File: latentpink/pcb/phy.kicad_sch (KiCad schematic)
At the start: 72 parts, among them J1 CONN_SFP_HOST, J18 BEL_FUSE_0845-2R1T-E4, J19 BEL_FUSE_0845-2R1T-E4, J2 SFP_CAGE, J20 BEL_FUSE_0845-2R1T-E4, J21 BEL_FUSE_0845-2R1T-E4, J3 XILINX_JTAG, J4 BEL_FUSE_0845-2R1T-E4, J8 BEL_FUSE_0845-2R1T-E4, M1 960-27-12-D-AB-0, U1 VSC8512, U2 XC7K160T-2FBG484C, U24 OSC_LVDS, U25 OSC_LVDS, U4 STM32H735-UFBGA176-25

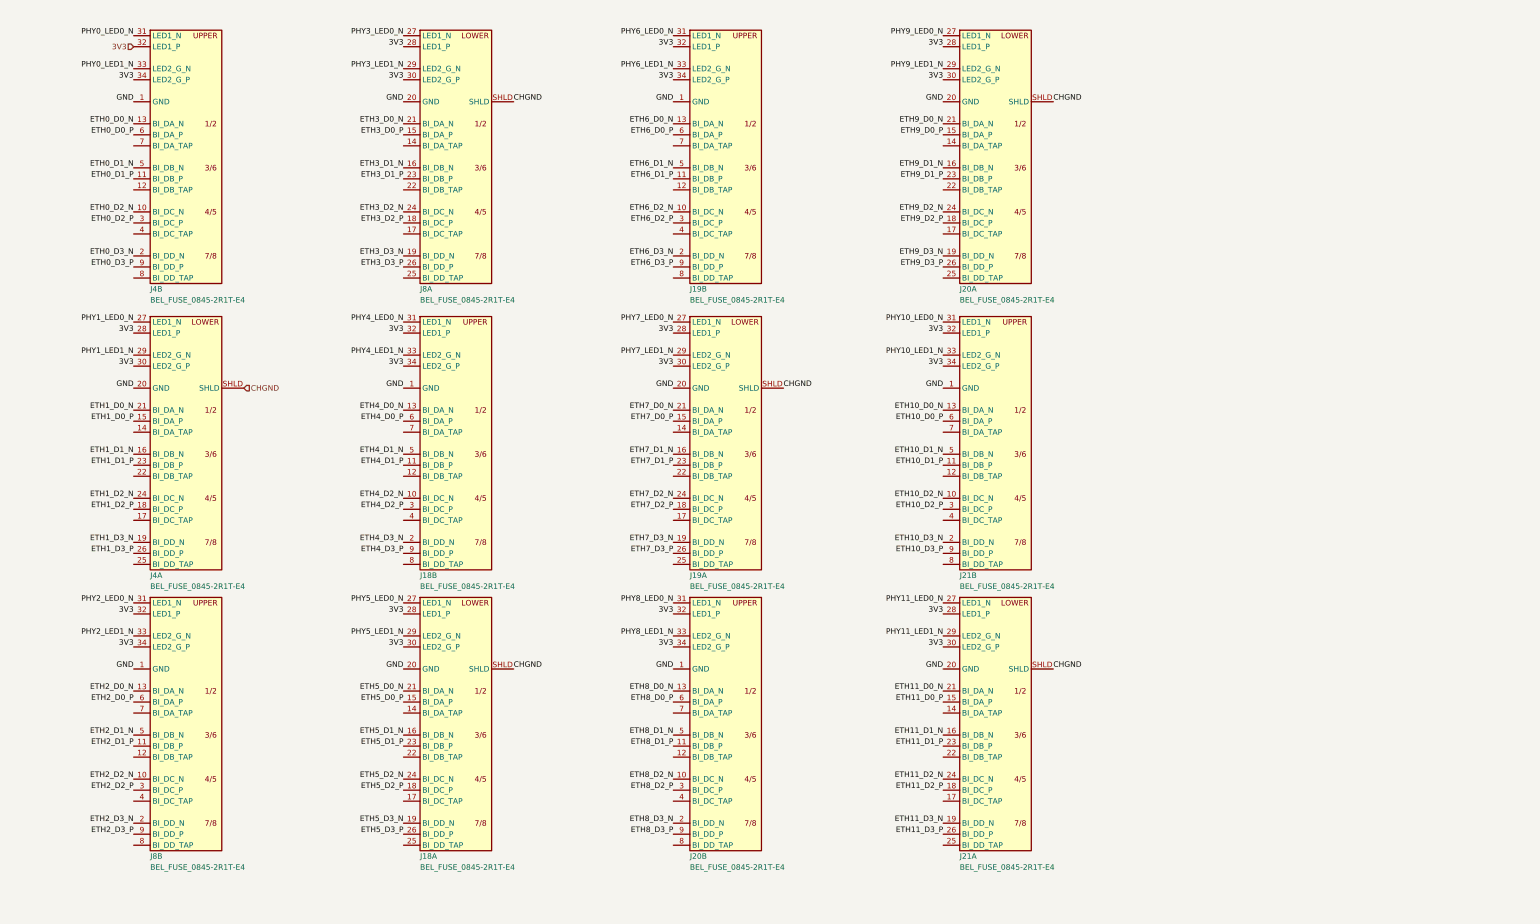
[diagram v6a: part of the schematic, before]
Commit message: Rearranged ports, added center tap capacitors
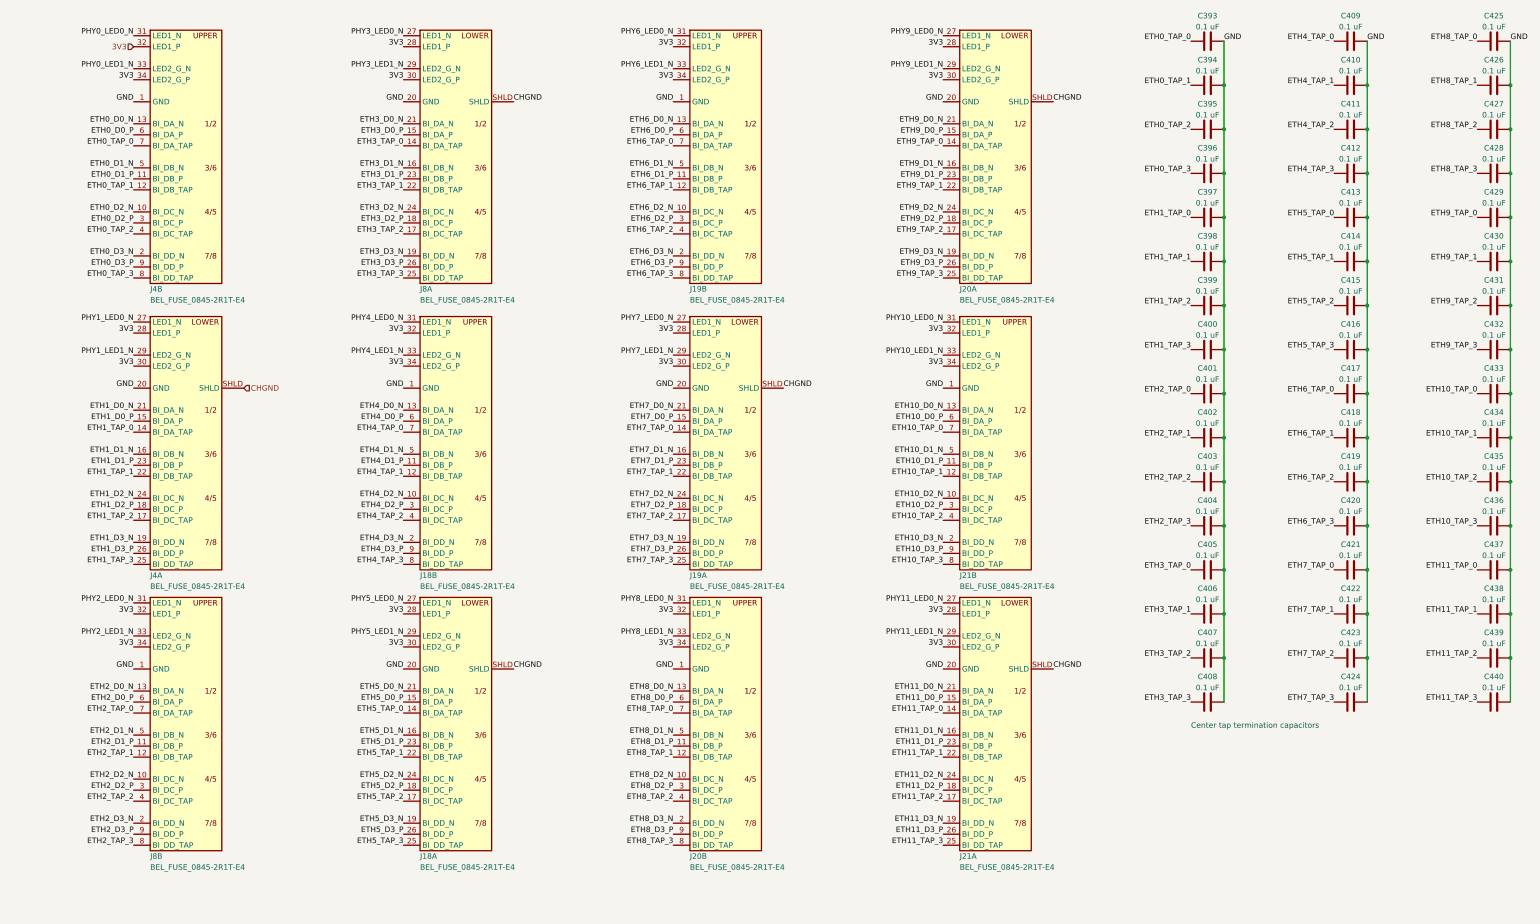
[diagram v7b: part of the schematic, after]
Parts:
- added C393, C394, C395, C396, C397, C398, C399, C400, C401, C402, C403, C404, C405, C406, C407, C408, C409, C410, C411, C412, C413, C414, C415, C416, C417, C418, C419, C420, C421, C422, C423, C424, C425, C426, C427, C428, C429, C430, C431, C432, C433, C434, C435, C436, C437, C438, C439, C440: 0.1 uF, azonenberg_pcb:EIA_0402_CAP_NOSILK, symbol device:C
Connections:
- net GND: now also C393.1, C394.1, C395.1, C396.1, C397.1, C398.1, C399.1, C400.1, C401.1, C402.1, C403.1, C404.1, C405.1, C406.1, C407.1, C408.1, C409.1, C410.1, C411.1, C412.1, C413.1, C414.1, C415.1, C416.1, C417.1, C418.1, C419.1, C420.1, C421.1, C422.1, C423.1, C424.1, C425.1, C426.1, C427.1, C428.1, C429.1, C430.1, C431.1, C432.1, C433.1, C434.1, C435.1, C436.1, C437.1, C438.1, C439.1, C440.1
- net ETH0_TAP_1: now reaches J4.12 (BI_DB_TAP)
- net ETH0_TAP_1: now also C394.2
- net ETH0_TAP_2: now reaches J4.4 (BI_DC_TAP)
- net ETH0_TAP_2: now also C395.2
- net ETH0_TAP_0: now reaches J4.7 (BI_DA_TAP)
- net ETH0_TAP_0: now also C393.2
- net ETH0_TAP_3: now reaches J4.8 (BI_DD_TAP)
- net ETH0_TAP_3: now also C396.2
- net ETH10_TAP_1: now reaches J21.12 (BI_DB_TAP)
- net ETH10_TAP_1: now also C434.2
- net ETH10_TAP_2: now reaches J21.4 (BI_DC_TAP)
- net ETH10_TAP_2: now also C435.2
- net ETH10_TAP_0: now reaches J21.7 (BI_DA_TAP)
- net ETH10_TAP_0: now also C433.2
- net ETH10_TAP_3: now reaches J21.8 (BI_DD_TAP)
- net ETH10_TAP_3: now also C436.2
- net ETH8_TAP_1: now reaches J20.12 (BI_DB_TAP)
- net ETH8_TAP_1: now also C426.2
- net ETH8_TAP_2: now reaches J20.4 (BI_DC_TAP)
- net ETH8_TAP_2: now also C427.2
- net ETH8_TAP_0: now reaches J20.7 (BI_DA_TAP)
- net ETH8_TAP_0: now also C425.2
- net ETH8_TAP_3: now reaches J20.8 (BI_DD_TAP)
- net ETH8_TAP_3: now also C428.2
- net ETH2_TAP_1: now reaches J8.12 (BI_DB_TAP)
- net ETH2_TAP_1: now also C402.2
- net ETH2_TAP_2: now reaches J8.4 (BI_DC_TAP)
- net ETH2_TAP_2: now also C403.2
- net ETH2_TAP_0: now reaches J8.7 (BI_DA_TAP)
- net ETH2_TAP_0: now also C401.2
- net ETH2_TAP_3: now reaches J8.8 (BI_DD_TAP)
- net ETH2_TAP_3: now also C404.2
- net ETH3_TAP_0: now reaches J8.14 (BI_DA_TAP)
- net ETH3_TAP_0: now also C405.2
- net ETH3_TAP_2: now reaches J8.17 (BI_DC_TAP)
- net ETH3_TAP_2: now also C407.2
- net ETH3_TAP_1: now reaches J8.22 (BI_DB_TAP)
- net ETH3_TAP_1: now also C406.2
- net ETH3_TAP_3: now reaches J8.25 (BI_DD_TAP)
- net ETH3_TAP_3: now also C408.2
- net ETH5_TAP_0: now reaches J18.14 (BI_DA_TAP)
- net ETH5_TAP_0: now also C413.2
- net ETH5_TAP_2: now reaches J18.17 (BI_DC_TAP)
- net ETH5_TAP_2: now also C415.2
- net ETH5_TAP_1: now reaches J18.22 (BI_DB_TAP)
- net ETH5_TAP_1: now also C414.2
- net ETH5_TAP_3: now reaches J18.25 (BI_DD_TAP)
- net ETH5_TAP_3: now also C416.2
- net ETH6_TAP_1: now reaches J19.12 (BI_DB_TAP)
- net ETH6_TAP_1: now also C418.2
- net ETH6_TAP_2: now reaches J19.4 (BI_DC_TAP)
- net ETH6_TAP_2: now also C419.2
- net ETH6_TAP_0: now reaches J19.7 (BI_DA_TAP)
- net ETH6_TAP_0: now also C417.2
- net ETH6_TAP_3: now reaches J19.8 (BI_DD_TAP)
- net ETH6_TAP_3: now also C420.2
- net ETH4_TAP_1: now reaches J18.12 (BI_DB_TAP)
- net ETH4_TAP_1: now also C410.2
- net ETH4_TAP_2: now reaches J18.4 (BI_DC_TAP)
- net ETH4_TAP_2: now also C411.2
- net ETH4_TAP_0: now reaches J18.7 (BI_DA_TAP)
- net ETH4_TAP_0: now also C409.2
- net ETH4_TAP_3: now reaches J18.8 (BI_DD_TAP)
- net ETH4_TAP_3: now also C412.2
- net ETH1_TAP_0: now reaches J4.14 (BI_DA_TAP)
- net ETH1_TAP_0: now also C397.2
- net ETH1_TAP_2: now reaches J4.17 (BI_DC_TAP)
- net ETH1_TAP_2: now also C399.2
- net ETH1_TAP_1: now reaches J4.22 (BI_DB_TAP)
- net ETH1_TAP_1: now also C398.2
- net ETH1_TAP_3: now reaches J4.25 (BI_DD_TAP)
- net ETH1_TAP_3: now also C400.2
- net ETH9_TAP_0: now reaches J20.14 (BI_DA_TAP)
- net ETH9_TAP_0: now also C429.2
- net ETH9_TAP_2: now reaches J20.17 (BI_DC_TAP)
- net ETH9_TAP_2: now also C431.2
- net ETH9_TAP_1: now reaches J20.22 (BI_DB_TAP)
- net ETH9_TAP_1: now also C430.2
- net ETH9_TAP_3: now reaches J20.25 (BI_DD_TAP)
- net ETH9_TAP_3: now also C432.2
- net ETH7_TAP_0: now reaches J19.14 (BI_DA_TAP)
- net ETH7_TAP_0: now also C421.2
- net ETH7_TAP_2: now reaches J19.17 (BI_DC_TAP)
- net ETH7_TAP_2: now also C423.2
- net ETH7_TAP_1: now reaches J19.22 (BI_DB_TAP)
- net ETH7_TAP_1: now also C422.2
- net ETH7_TAP_3: now reaches J19.25 (BI_DD_TAP)
- net ETH7_TAP_3: now also C424.2
- net ETH11_TAP_0: now reaches J21.14 (BI_DA_TAP)
- net ETH11_TAP_0: now also C437.2
- net ETH11_TAP_2: now reaches J21.17 (BI_DC_TAP)
- net ETH11_TAP_2: now also C439.2
- net ETH11_TAP_1: now reaches J21.22 (BI_DB_TAP)
- net ETH11_TAP_1: now also C438.2
- net ETH11_TAP_3: now reaches J21.25 (BI_DD_TAP)
- net ETH11_TAP_3: now also C440.2
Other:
- note added: "Center tap termination capacitors"

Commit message: Continued footprint assignment and miscellaneous missing tidbits of schematic
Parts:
- added C458, C459, C460, C461, C462, C463, C464, C465, C466: 0.47 uF, azonenberg_pcb:EIA_0402_CAP_NOSILK, symbol device:C
- added C467, C468, C469, C470, C473, C474: 0.1 uF, azonenberg_pcb:EIA_0402_CAP_NOSILK, symbol device:C
- added C471, C472: 22 uF, azonenberg_pcb:EIA_1206_CAP_NOSILK, symbol device:C
- added L6, L7: 4.7 uH, azonenberg_pcb:EIA_0805_INDUCTOR_NOSILK, symbol passive-azonenberg:INDUCTOR_PWROUT
- added R132, R133: 4.7K, azonenberg_pcb:EIA_0402_RES_NOSILK, symbol device:R
- added R134: 0.1, azonenberg_pcb:EIA_0402_RES_NOSILK, symbol device:R
- added R135, R136: 0.5, azonenberg_pcb:EIA_0402_RES_NOSILK, symbol device:R
- added U31, U32, U33, U34: 74LVC1T45, azonenberg_pcb:DFN_6_0.5MM_1.45x1.00MM, symbol special-azonenberg:74LVC1T45
- added U35: SIT9121AC-2B2-33E125.000000, azonenberg_pcb:OSCILLATOR_LVDS_3.2x2.5, symbol osc-azonenberg:OSC_LVDS_NOPAD
- TP19, TP20: footprint (none) -> azonenberg_pcb:TESTPOINT_SMT_0.5MM
- U24: value OSC_LVDS -> SIT9121AI-2BF-XXS200.000000G; footprint (none) -> azonenberg_pcb:OSCILLATOR_LVDS_3.2x2.5; symbol osc-azonenberg:OSC_LVDS -> osc-azonenberg:OSC_LVDS_NOPAD
- U25: value OSC_LVDS -> SIT9121AI-2BF-XXS156.250000G; footprint (none) -> azonenberg_pcb:OSCILLATOR_LVDS_3.2x2.5; symbol osc-azonenberg:OSC_LVDS -> osc-azonenberg:OSC_LVDS_NOPAD
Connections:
- net 2V5: now also C462.1, C463.1, C464.1, C465.1, R132.2, R133.2, U31.6 (VCCB), U32.6 (VCCB), U33.6 (VCCB), U34.6 (VCCB)
- net 3V3: now also C344.1, C345.1, U24.1 (EN), U24.6 (VDD), U25.1 (EN), U25.6 (VDD), C466.1, R134.2, U35.1 (EN), U35.6 (VDD)
- net GND: now also C344.2, C345.2, U24.3 (GND), U25.3 (GND), C458.2, C459.2, C460.2, C461.2, C462.2, C463.2, C464.2, C465.2, C466.2, C469.2, C470.2, C473.2, C474.2, R135.1, R136.1, U31.2 (GND), U31.5 (DIR), U32.2 (GND), U32.5 (DIR), U33.2 (GND), U34.2 (GND), U35.3 (GND)
- net GTX_REFCLK_156M25_N: now also C343.2
- net GTX_REFCLK_156M25_P: now also C342.2
- net GTX_REFCLK_SPARE_N: now also C341.2
- net GTX_REFCLK_SPARE_P: now also C340.2
- net SFP_VDD_RX: now also C471.1, C473.1, L6.1
- net SFP_VDD_TX: now also C472.1, C474.1, L7.1
- net VSC_FAST_STATUS: now also U31.4 (B)
- net VSC_MDC: now also U33.4 (B)
- net VSC_MDINT: now also R133.1, U32.4 (B)
- net VSC_MDIO: now also R132.1, U34.4 (B)
- net at C341.1: now also U24.5 (OUT_N)
- net at U25.4 (OUT_P): now also C342.1
- net at U25.5 (OUT_N): now also C343.1
- net PHY_REFCLK_125MHZ_N: now reaches U1.AA8 (REFCLK_N)
- net PHY_REFCLK_125MHZ_N: now also C468.2
- net PHY_REFCLK_125MHZ_P: now reaches U1.Y8 (REFCLK_P)
- net PHY_REFCLK_125MHZ_P: now also C467.2
- net at U24.4 (OUT_P): now also C340.1
- new net: C469.1, C470.1, L6.2, L7.2, R134.1
- new net: C471.2, R135.2
- new net: C468.1, U35.5 (OUT_N)
- new net: C467.1, U35.4 (OUT_P)
- new net: C472.2, R136.2
- new net 1V8_IO: C458.1, C459.1, C460.1, C461.1, U31.1 (VCCA), U32.1 (VCCA), U33.1 (VCCA), U33.5 (DIR), U34.1 (VCCA)
- new net VSC_FAST_STATUS_1V8: U31.3 (A)
- new net VSC_MDC_1V8: U33.3 (A)
- new net VSC_MDINT_1V8: U32.3 (A)
- new net VSC_MDIO_1V8: U34.3 (A)
- new net VSC_MDIO_OE: U34.5 (DIR)
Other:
- note added: "Can use 156.25 for both Provide a second oscillator footprint just in case"
- note added: "Level shifting for LVCMOS25 GPIOs to FPGA"
- note added: "Refclk is LVDS (must be AC coupled) and internally terminated / biased (Fig. 12 on page 16)"
- note added: "SFP+ power filtering"
- note removed: "TODO: LVCMOS25 I/Os to FPGA Need level shifting"
- note removed: "TODO: SFP power"
- note removed: "TODO: refclks Can use 156.25 for both, provide a second DNP oscillator just in case"
- note removed: "TODO: what is voltage range of refclk? is it internally terminated?"
- moved on the sheet: C340, C341, C342, C343, C344, C345
